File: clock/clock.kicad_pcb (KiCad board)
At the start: 2 copper layers, 176.8 x 81.3 mm, 278 parts, among them P101 CONN_01X03, P102 CONN_FAN_PWM, P103 XG4A-1631, P301 MCRF, Q201 MMBT3904, U201 PCA9306, U202 DAC8830, U203 LMV722, U204 LTC2990, U205 LP3853, U207 NC7SZ125, U301 Adafruit746, U302 MIC5225, U303 PA6H, U401 74LVC541, U501 TPS56428, U502 TPS56428, U503 TPS56428, U601 ADT7410, U602 DS3231, U603 ADT7410, Y202 CX210

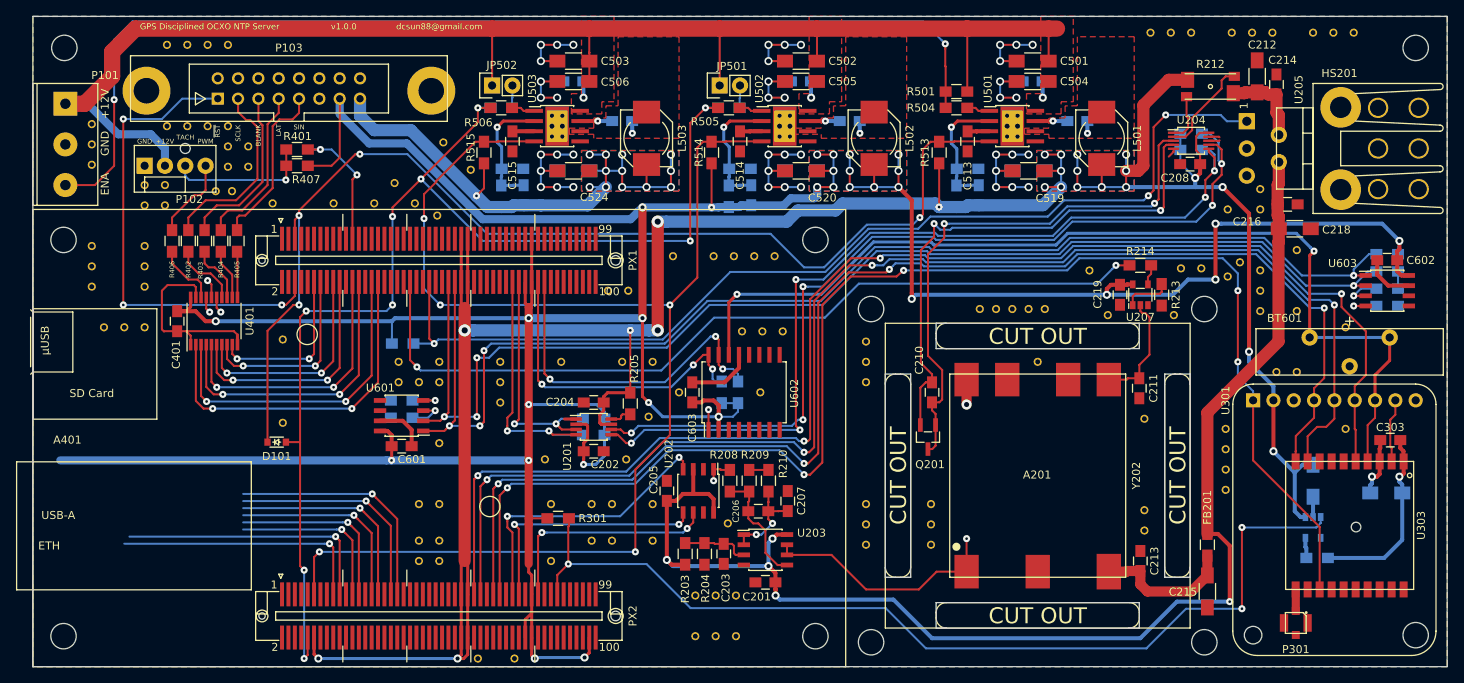
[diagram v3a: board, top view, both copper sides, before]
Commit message: Add expansion connector, 8 GPIO pins and power.
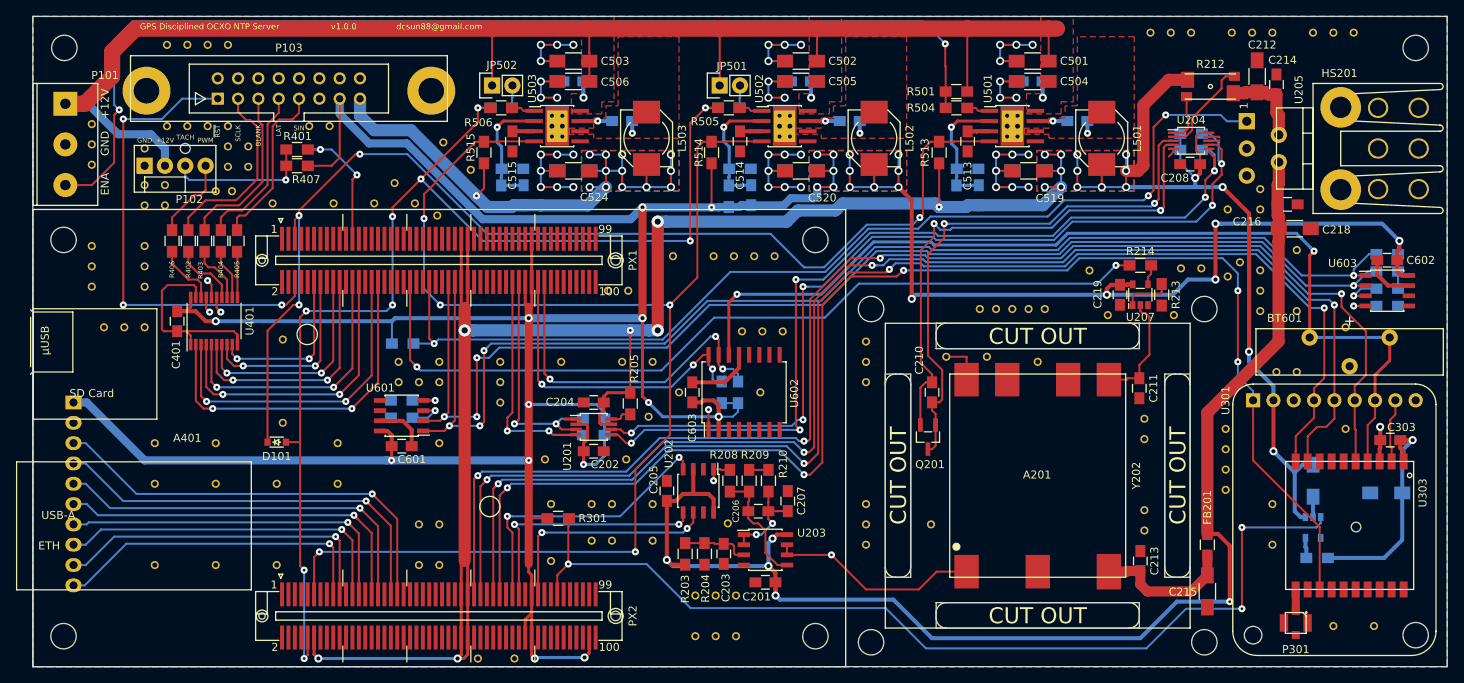
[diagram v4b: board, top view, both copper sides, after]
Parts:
- removed the REF** at (302.8, 231.1)
- removed the REF** at (302.8, 226.1)
- removed the REF** at (238.8, 226.1)
- removed the REF** at (241.3, 226.1)
- added P401: CONN_01X10, Pin_Headers:Pin_Header_Angled_1x10, B.Cu at (195.6, 213.4)
- added REF**: Stitching_Via_40x24mil, local:Stitching_Via_40x24mil, F.Cu at (227.6, 178.8)
- added REF**: Stitching_Via_40x24mil, local:Stitching_Via_40x24mil, F.Cu at (228.6, 218.4)
- added REF**: Stitching_Via_40x24mil, local:Stitching_Via_40x24mil, F.Cu at (228.6, 223.5)
- added REF**: Stitching_Via_40x24mil, local:Stitching_Via_40x24mil, F.Cu at (329.4, 217.9)
- added REF**: Stitching_Via_40x24mil, local:Stitching_Via_40x24mil, F.Cu at (221.0, 233.7)
- added REF**: Stitching_Via_40x24mil, local:Stitching_Via_40x24mil, F.Cu at (213.4, 233.7)
- added REF**: Stitching_Via_40x24mil, local:Stitching_Via_40x24mil, F.Cu at (205.7, 233.7)
- added REF**: Stitching_Via_40x24mil, local:Stitching_Via_40x24mil, F.Cu at (205.7, 218.4)
- added REF**: Stitching_Via_40x24mil, local:Stitching_Via_40x24mil, F.Cu at (213.4, 218.4)
- added REF**: Stitching_Via_40x24mil, local:Stitching_Via_40x24mil, F.Cu at (213.4, 223.5)
- added REF**: Stitching_Via_40x24mil, local:Stitching_Via_40x24mil, F.Cu at (221.0, 223.5)
- added REF**: Stitching_Via_40x24mil, local:Stitching_Via_40x24mil, F.Cu at (225.0, 178.8)
- added REF**: Stitching_Via_40x24mil, local:Stitching_Via_40x24mil, F.Cu at (205.7, 223.5)
- added REF**: Stitching_Via_40x24mil, local:Stitching_Via_40x24mil, F.Cu at (204.5, 181.6)
- added REF**: Stitching_Via_40x24mil, local:Stitching_Via_40x24mil, F.Cu at (304.7, 207.6)
- added REF**: Stitching_Via_40x24mil, local:Stitching_Via_40x24mil, F.Cu at (309.8, 207.6)
- added REF**: Stitching_Via_40x24mil, local:Stitching_Via_40x24mil, F.Cu at (345.4, 226.1)
- added REF**: Stitching_Via_40x24mil, local:Stitching_Via_40x24mil, F.Cu at (345.4, 231.1)
- added REF**: Stitching_Via_40x24mil, local:Stitching_Via_40x24mil, F.Cu at (358.1, 241.3)
- added REF**: Stitching_Via_40x24mil, local:Stitching_Via_40x24mil, F.Cu at (353.1, 241.3)
- moved REF** 2.03 mm to (238.8, 228.6)
- moved REF** 2.03 mm to (241.3, 228.6)
- moved REF** 0.51 mm to (241.3, 233.7)
- moved REF** 0.51 mm to (238.8, 233.7)
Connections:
- PX2 pad 17: /microzed/PX2_LVDS_0_P -> /microzed/GPIO7
- PX2 pad 19: /microzed/PX2_LVDS_0_N -> /microzed/GPIO6
- PX2 pad 23: /microzed/PX2_LVDS_2_P -> /microzed/GPIO5
- PX2 pad 25: /microzed/PX2_LVDS_2_N -> /microzed/GPIO4
- PX2 pad 29: /microzed/PX2_LVDS_4_P -> /microzed/GPIO3
- PX2 pad 31: /microzed/PX2_LVDS_4_N -> /microzed/GPIO2
- PX2 pad 35: /microzed/PX2_LVDS_6_P -> /microzed/GPIO1
- PX2 pad 37: /microzed/PX2_LVDS_6_N -> /microzed/GPIO0
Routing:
- net /microzed/GPIO0: track 0.00 -> 53.8 mm, vias 0 -> 1
- net /microzed/GPIO1: track 0.00 -> 51.5 mm, vias 0 -> 1
- net /microzed/GPIO2: track 0.00 -> 48.8 mm, vias 0 -> 1
- net /microzed/GPIO3: track 0.00 -> 46.4 mm, vias 0 -> 1
- net /microzed/GPIO4: track 0.00 -> 44.0 mm, vias 0 -> 1
- net /microzed/GPIO5: track 0.00 -> 43.0 mm, vias 0 -> 1
- net /microzed/GPIO6: track 0.00 -> 41.7 mm, vias 0 -> 1
- net /microzed/GPIO7: track 0.00 -> 40.7 mm, vias 0 -> 1
- net /microzed/PX2_LVDS_0_N: track 33.2 -> 0.00 mm, vias 1 -> 0
- net /microzed/PX2_LVDS_0_P: track 32.2 -> 0.00 mm, vias 1 -> 0
- net /microzed/PX2_LVDS_6_N: track 30.0 -> 0.00 mm, vias 1 -> 0
- net /microzed/PX2_LVDS_6_P: track 28.3 -> 0.00 mm, vias 1 -> 0
- net /microzed/PX2_LVDS_4_N: track 26.3 -> 0.00 mm, vias 1 -> 0
- net /microzed/PX2_LVDS_4_P: track 24.6 -> 0.00 mm, vias 1 -> 0
- net /microzed/PX2_LVDS_2_N: track 22.6 -> 0.00 mm, vias 1 -> 0
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
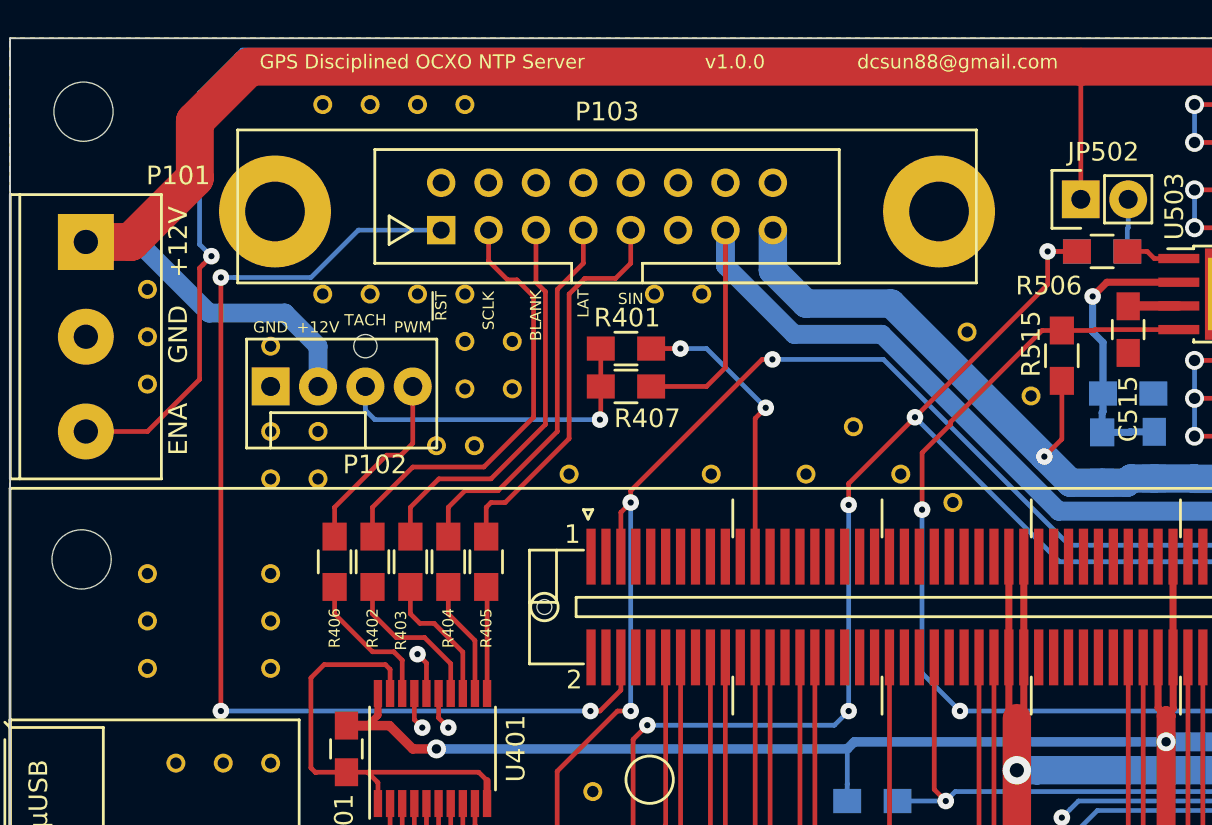
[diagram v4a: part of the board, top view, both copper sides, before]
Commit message: Turn off silk on pad.
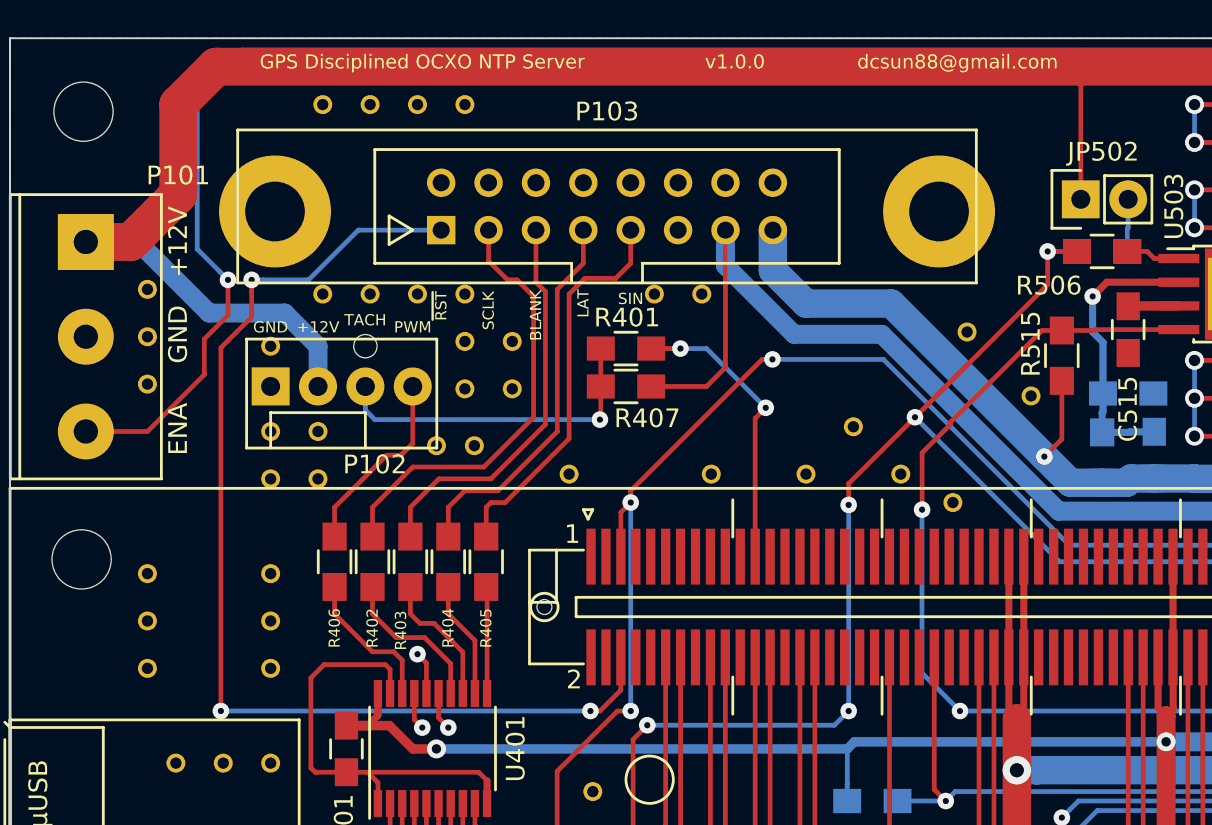
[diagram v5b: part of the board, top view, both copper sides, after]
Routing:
- net /power/+12V: track 189.8 -> 190.8 mm
- net /microzed/~CARRIER_SRST~: track 59.8 -> 58.7 mm
- net /power/+5V_ENA: track 137.2 -> 138.0 mm
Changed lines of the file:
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@@
     (links 568)
     (no_connects 0)
-    (area 190.449999 165.049999 367.334001 246.430001)
+    (area 184.650999 163.286 373.199858 248.171)
     (thickness 1.6)
     (drawings 70)
-    (tracks 1569)
+    (tracks 1573)
     (zones 0)
     (modules 295)
@@
     (mod_text_size 1 1)
     (mod_text_width 0.15)
-    (pad_size 3.048 4.191)
-    (pad_drill 0)
+    (pad_size 3 3)
+    (pad_drill 1.3)
     (pad_to_mask_clearance 0)
     (aux_axis_origin 0 0)
@@
     (fp_line (start 7.62 -4.05) (end -7.62 -4.05) (layer F.SilkS) (width 0.15))
     (fp_line (start -7.62 -4.05) (end -7.62 4.05) (layer F.SilkS) (width 0.15))
-    (pad 1 thru_hole rect (at -5.08 0 270) (size 3 3) (drill 1.3) (layers *.Cu *.Mask F.SilkS)
+    (pad 1 thru_hole rect (at -5.08 0 270) (size 3 3) (drill 1.3) (layers *.Cu *.Mask)
       (net 128 /power/+12V))
-    (pad 2 thru_hole circle (at 0 0 270) (size 3 3) (drill 1.3) (layers *.Cu *.Mask F.SilkS)
+    (pad 2 thru_hole circle (at 0 0 270) (size 3 3) (drill 1.3) (layers *.Cu *.Mask)
       (net 2 GND) (thermal_width 1.016))
-    (pad 3 thru_hole circle (at 5.08 0 270) (size 3 3) (drill 1.3) (layers *.Cu *.Mask F.SilkS)
+    (pad 3 thru_hole circle (at 5.08 0 270) (size 3 3) (drill 1.3) (layers *.Cu *.Mask)
       (net 32 /power/+5V_ENA))
     (model /home/guest/cae/kicad/mod/local.pretty/packages3d/1729131.wrl
@@
     (pad 1 thru_hole circle (at -5 0 180) (size 2.04 2.04) (drill 1.02) (layers *.Cu *.Mask)
       (net 54 /rtctemp/BATTERY))
+    (model /home/guest/cae/kicad/mod/local.pretty/packages3d/tmp/bk.wrl
+      (at (xyz 0 0 0))
+      (scale (xyz 0.393700787402 0.393700787402 0.393700787402))
+      (rotate (xyz 0 0 0))
+    )
   )
   (module local:MountingHole_125mil locked (layer F.Cu)
@@
     (pad 1 thru_hole rect (at -3.4036 8.2804 270) (size 2.032 2.032) (drill 1.143) (layers *.Cu *.Mask)
       (net 47 /ocxo/ENA))
-    (pad 5 thru_hole circle (at 3.4036 8.2804 270) (size 2.032 2.032) (drill 1.143) (layers *.Cu *.Mask F.SilkS)
+    (pad 5 thru_hole circle (at 3.4036 8.2804 270) (size 2.032 2.032) (drill 1.143) (layers *.Cu *.Mask)
       (net 53 "Net-(U205-Pad5)"))
     (pad 4 thru_hole circle (at 1.7018 4.2799 270) (size 2.032 2.032) (drill 1.143) (layers *.Cu *.Mask)
@@
   (segment (start 212.09 186.817) (end 212.09 183.769) (width 0.254) (layer F.Cu) (net 31) (status 20))
   (segment (start 194.564 186.182) (end 197.866 186.182) (width 0.254) (layer F.Cu) (net 32))
-  (segment (start 197.866 186.182) (end 200.660002 183.387998) (width 0.254) (layer F.Cu) (net 32))
-  (segment (start 200.660002 183.387998) (end 200.660002 177.418998) (width 0.254) (layer F.Cu) (net 32))
-  (segment (start 200.660002 177.418998) (end 200.850501 177.228499) (width 0.254) (layer F.Cu) (net 32))
-  (segment (start 200.850501 177.228499) (end 201.295 176.784) (width 0.254) (layer F.Cu) (net 32))
-  (segment (start 304.545992 168.529) (end 301.751992 165.735) (width 0.254) (layer B.Cu) (net 32))
+  (segment (start 197.866 186.182) (end 200.914 183.134) (width 0.254) (layer F.Cu) (net 32))
+  (segment (start 200.914 183.134) (end 200.914 181.229) (width 0.254) (layer F.Cu) (net 32))
+  (segment (start 200.914 181.229) (end 202.184 179.959) (width 0.254) (layer F.Cu) (net 32))
+  (segment (start 202.184 179.959) (end 202.184 178.054) (width 0.254) (layer F.Cu) (net 32))
+  (segment (start 200.533 168.148) (end 200.533 176.403) (width 0.254) (layer B.Cu) (net 32))
+  (segment (start 201.739501 177.609501) (end 202.184 178.054) (width 0.254) (layer B.Cu) (net 32))
+  (segment (start 202.946 165.735) (end 200.533 168.148) (width 0.254) (layer B.Cu) (net 32))
   (segment (start 301.751992 165.735) (end 202.946 165.735) (width 0.254) (layer B.Cu) (net 32))
-  (segment (start 202.946 165.735) (end 200.66 168.021) (width 0.254) (layer B.Cu) (net 32))
-  (segment (start 200.66 168.021) (end 200.66 176.149) (width 0.254) (layer B.Cu) (net 32))
-  (segment (start 200.66 176.149) (end 201.295 176.784) (width 0.254) (layer B.Cu) (net 32))
-  (via (at 201.295 176.784) (size 0.889) (drill 0.3302) (layers F.Cu B.Cu) (net 32))
+  (segment (start 200.533 176.403) (end 201.739501 177.609501) (width 0.254) (layer B.Cu) (net 32))
+  (segment (start 304.545992 168.529) (end 301.751992 165.735) (width 0.254) (layer B.Cu) (net 32))
+  (via (at 202.184 178.054) (size 0.889) (drill 0.3302) (layers F.Cu B.Cu) (net 32))
   (segment (start 304.546 171.323) (end 304.593 171.37) (width 0.254) (layer F.Cu) (net 32))
   (segment (start 304.593 171.37) (end 304.593 174.498) (width 0.254) (layer F.Cu) (net 32))
@@
   (segment (start 329.819 236.982) (end 335.312 236.982) (width 1.27) (layer F.Cu) (net 127))
   (segment (start 337.312 234.982) (end 337.312 232.49) (width 1.27) (layer F.Cu) (net 127) (status 30))
+  (segment (start 194.564 176.022) (end 196.977 176.022) (width 2.032) (layer F.Cu) (net 128))
+  (segment (start 196.977 176.022) (end 199.517 173.482) (width 2.032) (layer F.Cu) (net 128))
+  (segment (start 199.517 173.482) (end 199.517 168.656) (width 2.032) (layer F.Cu) (net 128))
+  (segment (start 199.517 168.656) (end 201.549 166.624) (width 2.032) (layer F.Cu) (net 128))
+  (segment (start 201.549 166.624) (end 247.904 166.624) (width 2.032) (layer F.Cu) (net 128))
   (segment (start 194.564 176.022) (end 197.358 176.022) (width 1.016) (layer B.Cu) (net 128))
   (segment (start 197.358 176.022) (end 201.168 179.832) (width 1.016) (layer B.Cu) (net 128))
@@
   (segment (start 276.352 166.631416) (end 276.344584 166.624) (width 0.254) (layer F.Cu) (net 128))
   (segment (start 307.271663 166.624) (end 307.293 166.645337) (width 2.032) (layer F.Cu) (net 128))
-  (segment (start 203.327 166.624) (end 247.904 166.624) (width 2.032) (layer F.Cu) (net 128))
   (segment (start 307.293 174.498) (end 307.293 166.645337) (width 0.254) (layer F.Cu) (net 128) (status 10))
   (segment (start 316.718 173.228) (end 316.718 175.24) (width 0.508) (layer B.Cu) (net 128) (status 10))
@@
   (segment (start 287.762 175.24) (end 287.782 175.26) (width 0.508) (layer B.Cu) (net 128))
   (via (at 287.782 175.26) (size 1.016) (drill 0.508) (layers F.Cu B.Cu) (net 128))
-  (segment (start 194.564 176.022) (end 196.977 176.022) (width 2.032) (layer F.Cu) (net 128) (status 10))
-  (segment (start 196.977 176.022) (end 200.406 172.593) (width 2.032) (layer F.Cu) (net 128))
-  (segment (start 200.406 169.545) (end 203.327 166.624) (width 2.032) (layer F.Cu) (net 128))
-  (segment (start 200.406 172.593) (end 200.406 169.545) (width 2.032) (layer F.Cu) (net 128))
   (segment (start 259.314 173.228) (end 259.314 175.24) (width 0.508) (layer B.Cu) (net 128) (status 10))
   (via (at 259.334 175.26) (size 1.016) (drill 0.508) (layers F.Cu B.Cu) (net 128))
@@
   (segment (start 260.064 173.228) (end 260.064 170.688) (width 0.254) (layer F.Cu) (net 128) (status 30))
   (segment (start 260.064 170.688) (end 260.223 170.529) (width 0.254) (layer F.Cu) (net 128) (status 30))
+  (segment (start 203.454 180.042436) (end 203.454 178.682617) (width 0.254) (layer F.Cu) (net 168))
+  (segment (start 201.803 181.693436) (end 203.454 180.042436) (width 0.254) (layer F.Cu) (net 168))
+  (segment (start 203.454 178.682617) (end 203.454 178.054) (width 0.254) (layer F.Cu) (net 168))
+  (segment (start 201.803 201.168) (end 201.803 181.693436) (width 0.254) (layer F.Cu) (net 168))
+  (segment (start 206.502 178.054) (end 204.082617 178.054) (width 0.254) (layer B.Cu) (net 168))
+  (segment (start 204.082617 178.054) (end 203.454 178.054) (width 0.254) (layer B.Cu) (net 168))
+  (segment (start 209.169 175.387) (end 206.502 178.054) (width 0.254) (layer B.Cu) (net 168))
   (segment (start 213.614 175.387) (end 209.169 175.387) (width 0.254) (layer B.Cu) (net 168))
-  (segment (start 209.169 175.387) (end 206.629 177.927) (width 0.254) (layer B.Cu) (net 168))
-  (segment (start 206.629 177.927) (end 202.565 177.927) (width 0.254) (layer B.Cu) (net 168))
-  (segment (start 202.565 177.927) (end 201.803 177.927) (width 0.254) (layer B.Cu) (net 168))
-  (segment (start 201.803 201.168) (end 201.803 177.927) (width 0.254) (layer F.Cu) (net 168))
-  (via (at 201.803 177.927) (size 0.889) (drill 0.3302) (layers F.Cu B.Cu) (net 168))
+  (via (at 203.454 178.054) (size 0.889) (drill 0.3302) (layers F.Cu B.Cu) (net 168))
   (segment (start 201.803016 201.167984) (end 201.803 201.168) (width 0.254) (layer B.Cu) (net 168))
   (segment (start 221.615 201.167984) (end 201.803016 201.167984) (width 0.254) (layer B.Cu) (net 168))
